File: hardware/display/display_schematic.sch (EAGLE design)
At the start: 23 parts, among them IC1 MCP2300X/P, IC2 4511N

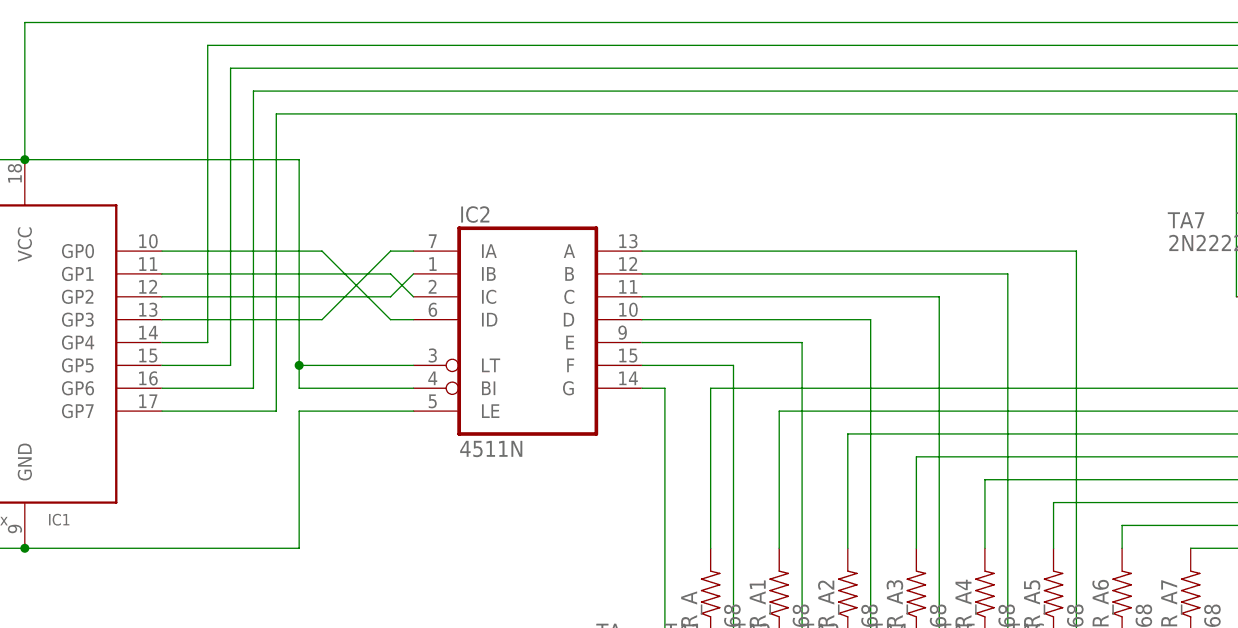
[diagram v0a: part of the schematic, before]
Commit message: Schematics Updating display schematic and adding schematics for ledarrows and servos. Also adding image exports for simplified illustration.
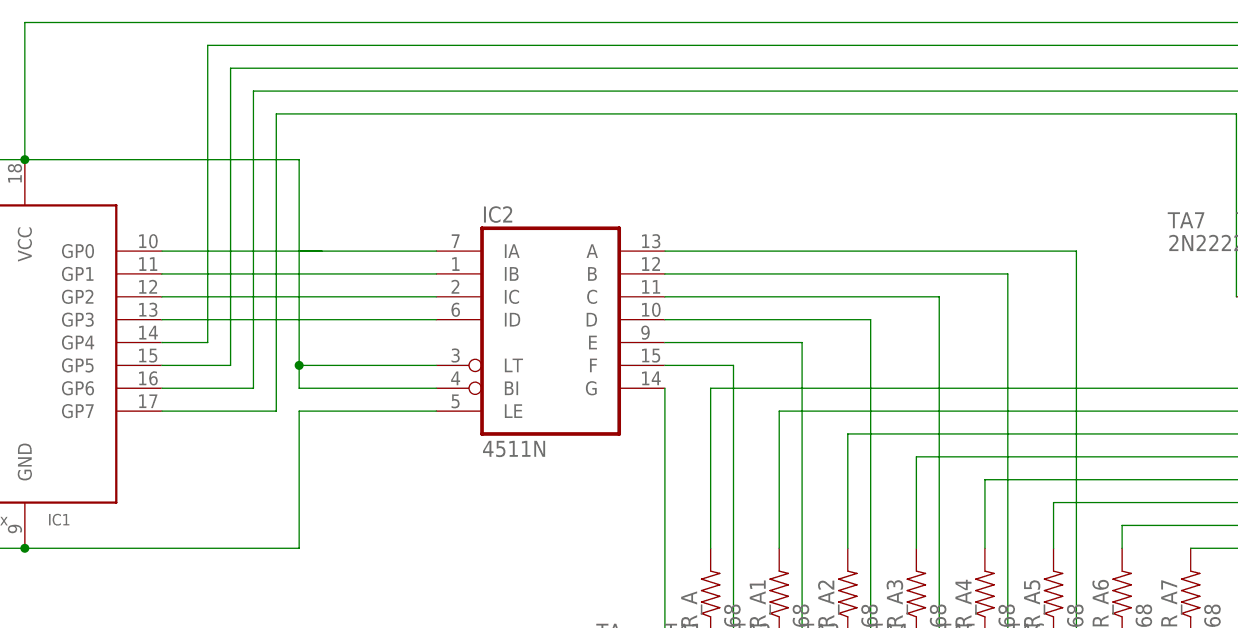
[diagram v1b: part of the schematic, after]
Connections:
- net N$1: now also IC2A.IA
- net N$10: no longer IC2A.ID
- net N$7: now also IC2A.ID; no longer IC2A.IA
- net N$8: now also IC2A.IB; no longer IC2A.IC
- net N$9: now also IC2A.IC; no longer IC2A.IB
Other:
- moved on the sheet: IC2
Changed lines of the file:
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@@
 <setting verticaltext="up"/>
 </settings>
-<grid distance="0.1" unitdist="inch" unit="inch" style="lines" multiple="1" display="yes" altdistance="0.01" altunitdist="inch" altunit="inch"/>
+<grid distance="0.1" unitdist="inch" unit="inch" style="lines" multiple="1" display="no" altdistance="0.01" altunitdist="inch" altunit="inch"/>
 <layers>
 <layer number="1" name="Top" color="4" fill="1" visible="no" active="no"/>
@@
 <instance part="IC1" gate="G$1" x="20.32" y="63.5"/>
 <instance part="JP1" gate="G$1" x="-15.24" y="60.96"/>
-<instance part="IC2" gate="A" x="76.2" y="66.04"/>
+<instance part="IC2" gate="A" x="78.74" y="66.04"/>
 <instance part="DISPLAY7S4D1" gate="G$1" x="200.66" y="40.64" rot="R270"/>
 <instance part="R_A" gate="G$1" x="96.52" y="35.56" rot="R90"/>
@@
 <wire x1="-5.08" y1="66.04" x2="-7.62" y2="66.04" width="0.1524" layer="91"/>
 <wire x1="20.32" y1="83.82" x2="50.8" y2="83.82" width="0.1524" layer="91"/>
-<wire x1="50.8" y1="83.82" x2="50.8" y2="60.96" width="0.1524" layer="91"/>
+<wire x1="50.8" y1="83.82" x2="50.8" y2="73.66" width="0.1524" layer="91"/>
 <pinref part="IC2" gate="A" pin="LT"/>
-<wire x1="50.8" y1="60.96" x2="63.5" y2="60.96" width="0.1524" layer="91"/>
+<wire x1="50.8" y1="73.66" x2="50.8" y2="60.96" width="0.1524" layer="91"/>
+<wire x1="50.8" y1="60.96" x2="66.04" y2="60.96" width="0.1524" layer="91"/>
 <wire x1="50.8" y1="60.96" x2="50.8" y2="58.42" width="0.1524" layer="91"/>
 <pinref part="IC2" gate="A" pin="BI"/>
-<wire x1="50.8" y1="58.42" x2="63.5" y2="58.42" width="0.1524" layer="91"/>
+<wire x1="50.8" y1="58.42" x2="66.04" y2="58.42" width="0.1524" layer="91"/>
 <junction x="20.32" y="83.82"/>
 <junction x="50.8" y="60.96"/>
@@
 <junction x="167.64" y="99.06"/>
 <junction x="175.26" y="99.06"/>
+<pinref part="IC2" gate="A" pin="IA"/>
+<wire x1="50.8" y1="73.66" x2="66.04" y2="73.66" width="0.1524" layer="91"/>
 </segment>
 </net>
@@
 <junction x="-5.08" y="50.8"/>
 <pinref part="IC2" gate="A" pin="LE"/>
-<wire x1="63.5" y1="55.88" x2="50.8" y2="55.88" width="0.1524" layer="91"/>
+<wire x1="66.04" y1="55.88" x2="50.8" y2="55.88" width="0.1524" layer="91"/>
 <wire x1="50.8" y1="55.88" x2="50.8" y2="40.64" width="0.1524" layer="91"/>
 <wire x1="50.8" y1="40.64" x2="20.32" y2="40.64" width="0.1524" layer="91"/>
@@
 </segment>
 </net>
-<net name="N$8" class="0">
-<segment>
-<pinref part="IC1" gate="G$1" pin="GP1"/>
-<pinref part="IC2" gate="A" pin="IC"/>
-<wire x1="35.56" y1="71.12" x2="60.96" y2="71.12" width="0.1524" layer="91"/>
-<wire x1="60.96" y1="71.12" x2="63.5" y2="68.58" width="0.1524" layer="91"/>
-</segment>
-</net>
-<net name="N$9" class="0">
-<segment>
-<pinref part="IC1" gate="G$1" pin="GP2"/>
-<pinref part="IC2" gate="A" pin="IB"/>
-<wire x1="35.56" y1="68.58" x2="60.96" y2="68.58" width="0.1524" layer="91"/>
-<wire x1="60.96" y1="68.58" x2="63.5" y2="71.12" width="0.1524" layer="91"/>
-</segment>
-</net>
 <net name="N$7" class="0">
 <segment>
-<pinref part="IC2" gate="A" pin="IA"/>
-<wire x1="63.5" y1="73.66" x2="60.96" y2="73.66" width="0.1524" layer="91"/>
-<wire x1="60.96" y1="73.66" x2="53.34" y2="66.04" width="0.1524" layer="91"/>
 <pinref part="IC1" gate="G$1" pin="GP3"/>
-<wire x1="53.34" y1="66.04" x2="35.56" y2="66.04" width="0.1524" layer="91"/>
+<pinref part="IC2" gate="A" pin="ID"/>
+<wire x1="66.04" y1="66.04" x2="35.56" y2="66.04" width="0.1524" layer="91"/>
 </segment>
 </net>
 <net name="N$10" class="0">
 <segment>
-<pinref part="IC2" gate="A" pin="ID"/>
-<wire x1="63.5" y1="66.04" x2="60.96" y2="66.04" width="0.1524" layer="91"/>
-<wire x1="60.96" y1="66.04" x2="53.34" y2="73.66" width="0.1524" layer="91"/>
 <pinref part="IC1" gate="G$1" pin="GP0"/>
 <wire x1="53.34" y1="73.66" x2="35.56" y2="73.66" width="0.1524" layer="91"/>
@@
 <segment>
 <pinref part="IC2" gate="A" pin="G"/>
-<wire x1="88.9" y1="58.42" x2="91.44" y2="58.42" width="0.1524" layer="91"/>
 <pinref part="TA" gate="G$1" pin="B"/>
 <wire x1="91.44" y1="58.42" x2="91.44" y2="22.86" width="0.1524" layer="91"/>
@@
 <pinref part="IC2" gate="A" pin="F"/>
 <pinref part="TA1" gate="G$1" pin="B"/>
-<wire x1="88.9" y1="60.96" x2="99.06" y2="60.96" width="0.1524" layer="91"/>
+<wire x1="91.44" y1="60.96" x2="99.06" y2="60.96" width="0.1524" layer="91"/>
 <wire x1="99.06" y1="60.96" x2="99.06" y2="22.86" width="0.1524" layer="91"/>
 </segment>
@@
 <segment>
 <pinref part="IC2" gate="A" pin="E"/>
-<wire x1="88.9" y1="63.5" x2="106.68" y2="63.5" width="0.1524" layer="91"/>
+<wire x1="91.44" y1="63.5" x2="106.68" y2="63.5" width="0.1524" layer="91"/>
 <pinref part="TA2" gate="G$1" pin="B"/>
 <wire x1="106.68" y1="63.5" x2="106.68" y2="22.86" width="0.1524" layer="91"/>
@@
 <segment>
 <pinref part="IC2" gate="A" pin="D"/>
-<wire x1="88.9" y1="66.04" x2="114.3" y2="66.04" width="0.1524" layer="91"/>
+<wire x1="91.44" y1="66.04" x2="114.3" y2="66.04" width="0.1524" layer="91"/>
 <pinref part="TA3" gate="G$1" pin="B"/>
 <wire x1="114.3" y1="66.04" x2="114.3" y2="22.86" width="0.1524" layer="91"/>
@@
 <segment>
 <pinref part="IC2" gate="A" pin="C"/>
-<wire x1="88.9" y1="68.58" x2="121.92" y2="68.58" width="0.1524" layer="91"/>
+<wire x1="91.44" y1="68.58" x2="121.92" y2="68.58" width="0.1524" layer="91"/>
 <pinref part="TA4" gate="G$1" pin="B"/>
 <wire x1="121.92" y1="68.58" x2="121.92" y2="22.86" width="0.1524" layer="91"/>
@@
 <pinref part="IC2" gate="A" pin="B"/>
 <pinref part="TA5" gate="G$1" pin="B"/>
-<wire x1="88.9" y1="71.12" x2="129.54" y2="71.12" width="0.1524" layer="91"/>
+<wire x1="91.44" y1="71.12" x2="129.54" y2="71.12" width="0.1524" layer="91"/>
 <wire x1="129.54" y1="71.12" x2="129.54" y2="22.86" width="0.1524" layer="91"/>
 </segment>
@@
 <pinref part="IC2" gate="A" pin="A"/>
 <pinref part="TA6" gate="G$1" pin="B"/>
-<wire x1="88.9" y1="73.66" x2="137.16" y2="73.66" width="0.1524" layer="91"/>
+<wire x1="91.44" y1="73.66" x2="137.16" y2="73.66" width="0.1524" layer="91"/>
 <wire x1="137.16" y1="73.66" x2="137.16" y2="22.86" width="0.1524" layer="91"/>
 </segment>
@@
 </segment>
 </net>
+<net name="N$8" class="0">
+<segment>
+<pinref part="IC1" gate="G$1" pin="GP1"/>
+<wire x1="35.56" y1="71.12" x2="66.04" y2="71.12" width="0.1524" layer="91"/>
+<pinref part="IC2" gate="A" pin="IB"/>
+</segment>
+</net>
+<net name="N$9" class="0">
+<segment>
+<pinref part="IC1" gate="G$1" pin="GP2"/>
+<wire x1="66.04" y1="68.58" x2="35.56" y2="68.58" width="0.1524" layer="91"/>
+<pinref part="IC2" gate="A" pin="IC"/>
+</segment>
+</net>

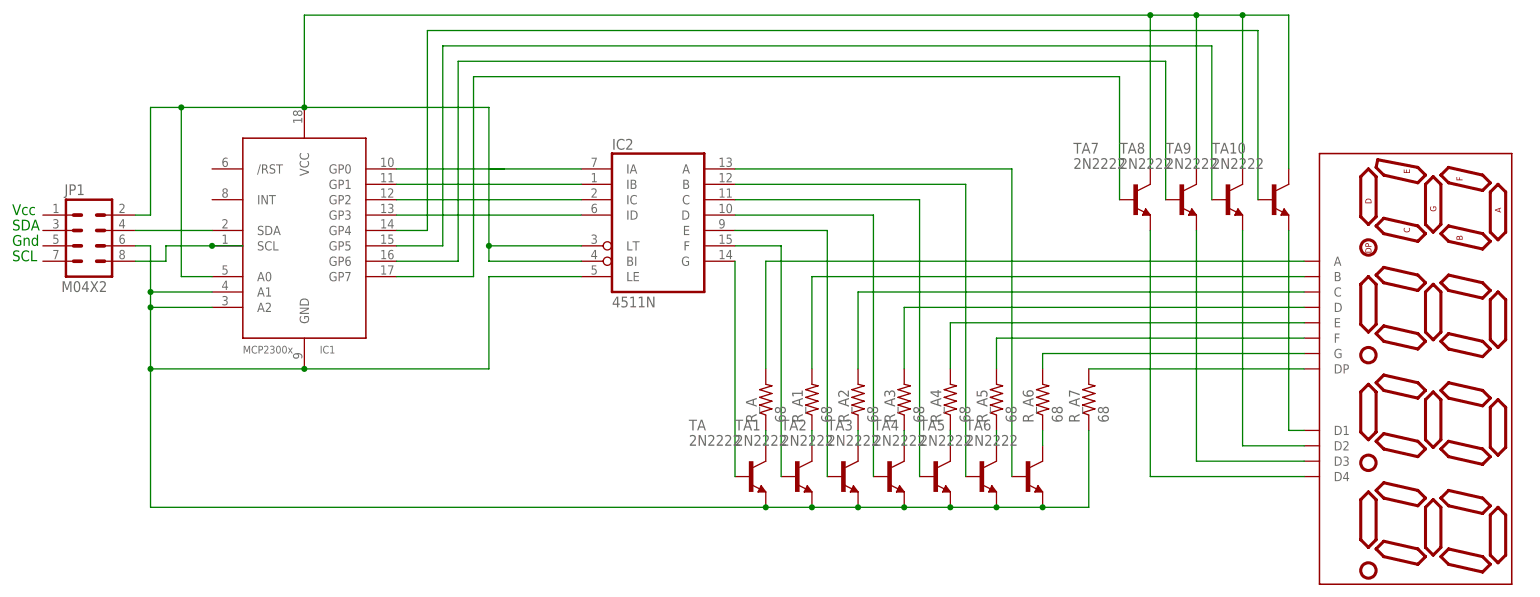
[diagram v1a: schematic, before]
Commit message: Schematics updates: Adding a shield schematic file for the microcontroller board header connector and power breakdown. Adding page border to existing schematics. Adding a few component values. Updating the display schematic to use common cathode 7 segment.
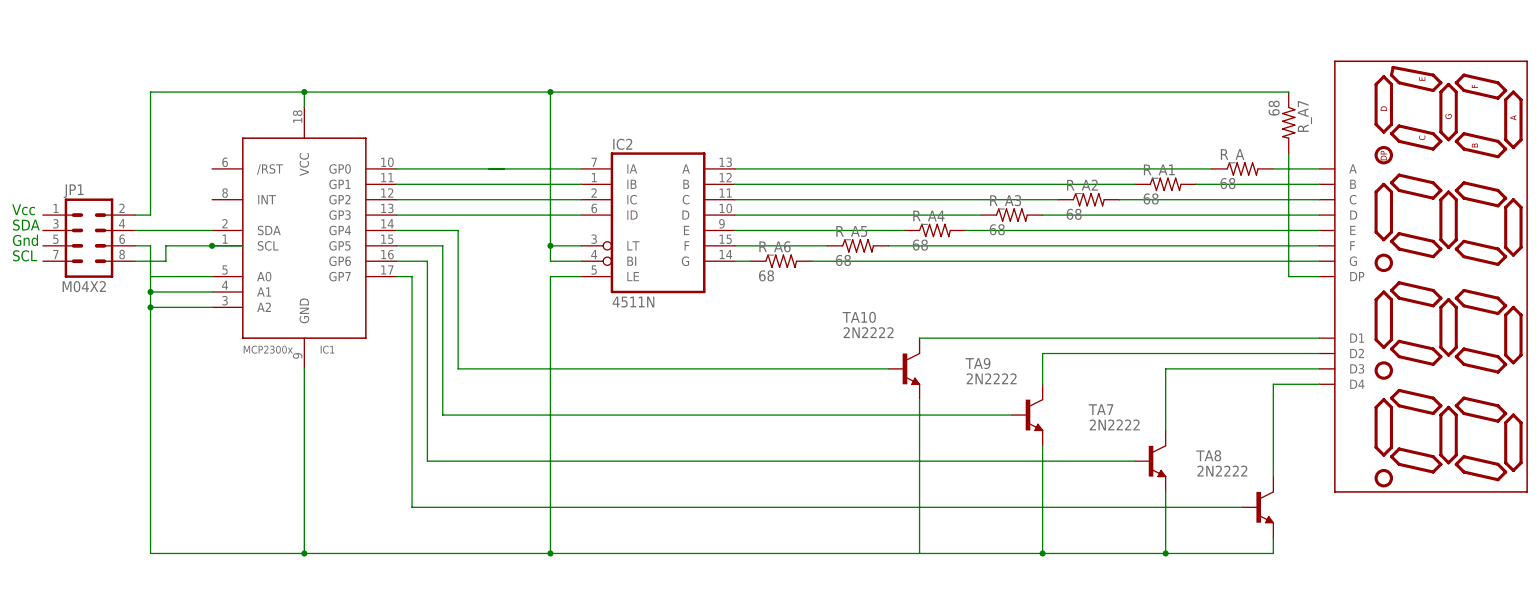
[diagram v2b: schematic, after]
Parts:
- removed TA, TA1, TA2, TA3, TA4, TA5, TA6: 2N2222, adafruit:2N2222
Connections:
- removed net N$42: DISPLAY7S4D1.D4, TA7.E
- removed net N$43: DISPLAY7S4D1.D3, TA8.E
- removed net N$44: DISPLAY7S4D1.D2, TA9.E
- removed net N$45: DISPLAY7S4D1.D1, TA10.E
- removed net TR_A: R_A.1, TA.C
- removed net TR_A1: R_A1.1, TA1.C
- removed net TR_A2: R_A2.1, TA2.C
- removed net TR_A3: R_A3.1, TA3.C
- removed net TR_A4: R_A4.1, TA4.C
- removed net TR_A5: R_A5.1, TA5.C
- removed net TR_A6: R_A6.1, TA6.C
- new net N$12: DISPLAY7S4D1.D1, TA10.C
- new net N$20: DISPLAY7S4D1.D4, TA8.C
- new net N$24: IC2A.IA
- new net N$29: IC1.GP7, TA8.B
- new net N$30: IC1.GP6, TA7.B
- net N$1: now also R_A7.1; no longer IC1.A0, IC2A.IA, TA10.C, TA7.C, TA8.C, TA9.C
- net N$13: now also DISPLAY7S4D1.D2, TA9.C; no longer IC1.GP6, TA8.B
- net N$14: now also R_A5.1; no longer TA1.B
- net N$16: now also R_A4.1; no longer TA2.B
- net N$19: now also DISPLAY7S4D1.D3, TA7.C; no longer IC1.GP7, TA7.B
- net N$2: now also IC1.A0, TA10.E, TA7.E, TA8.E, TA9.E; no longer R_A7.1, TA.E, TA1.E, TA2.E, TA3.E, TA4.E, TA5.E, TA6.E
- net N$27: now also R_A3.1; no longer TA3.B
- net N$28: now also R_A2.1; no longer TA4.B
- net N$39: now also R_A1.1; no longer TA5.B
- net N$40: now also R_A.1; no longer TA6.B
- net N$5: now also R_A6.1; no longer TA.B
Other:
- moved on the sheet: R_A, R_A1, R_A2, R_A3, R_A4, R_A5, R_A6, R_A7, TA10, TA7, TA8, TA9

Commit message: Updating the schematics to include A5 frames and complete some component values. Also adding the arduino shield symbol to the shield schematic.
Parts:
- added R_A10, R_A11, R_A8, R_A9: 68, SparkFun-Resistors:RESISTORAXIAL-0.3
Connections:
- new net N$23: R_A11.2, TA8.B
- new net N$32: R_A8.2, TA10.B
- new net N$33: R_A10.2, TA7.B
- net N$1: now also IC1./RST
- net N$10: now also IC2A.IA
- net N$2: now also JP1.8; no longer JP1.6
- net N$22: now also R_A8.1; no longer TA10.B
- net N$24: now also R_A9.2, TA9.B; no longer IC2A.IA
- net N$29: now also R_A11.1; no longer TA8.B
- net N$3: now also IC1.SCL; no longer IC1.SDA
- net N$30: now also R_A10.1; no longer TA7.B
- net N$31: now also R_A9.1; no longer TA9.B
- net N$4: now also JP1.6; no longer IC1.SCL, JP1.8
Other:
- moved on the sheet: IC1, JP1, TA8
